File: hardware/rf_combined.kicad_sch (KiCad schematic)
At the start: 16 parts, among them J7 Conn_Coaxial, U1 PAT1220-C-3DB, U10 COS358SR, U2 PAT1220-C-3DB

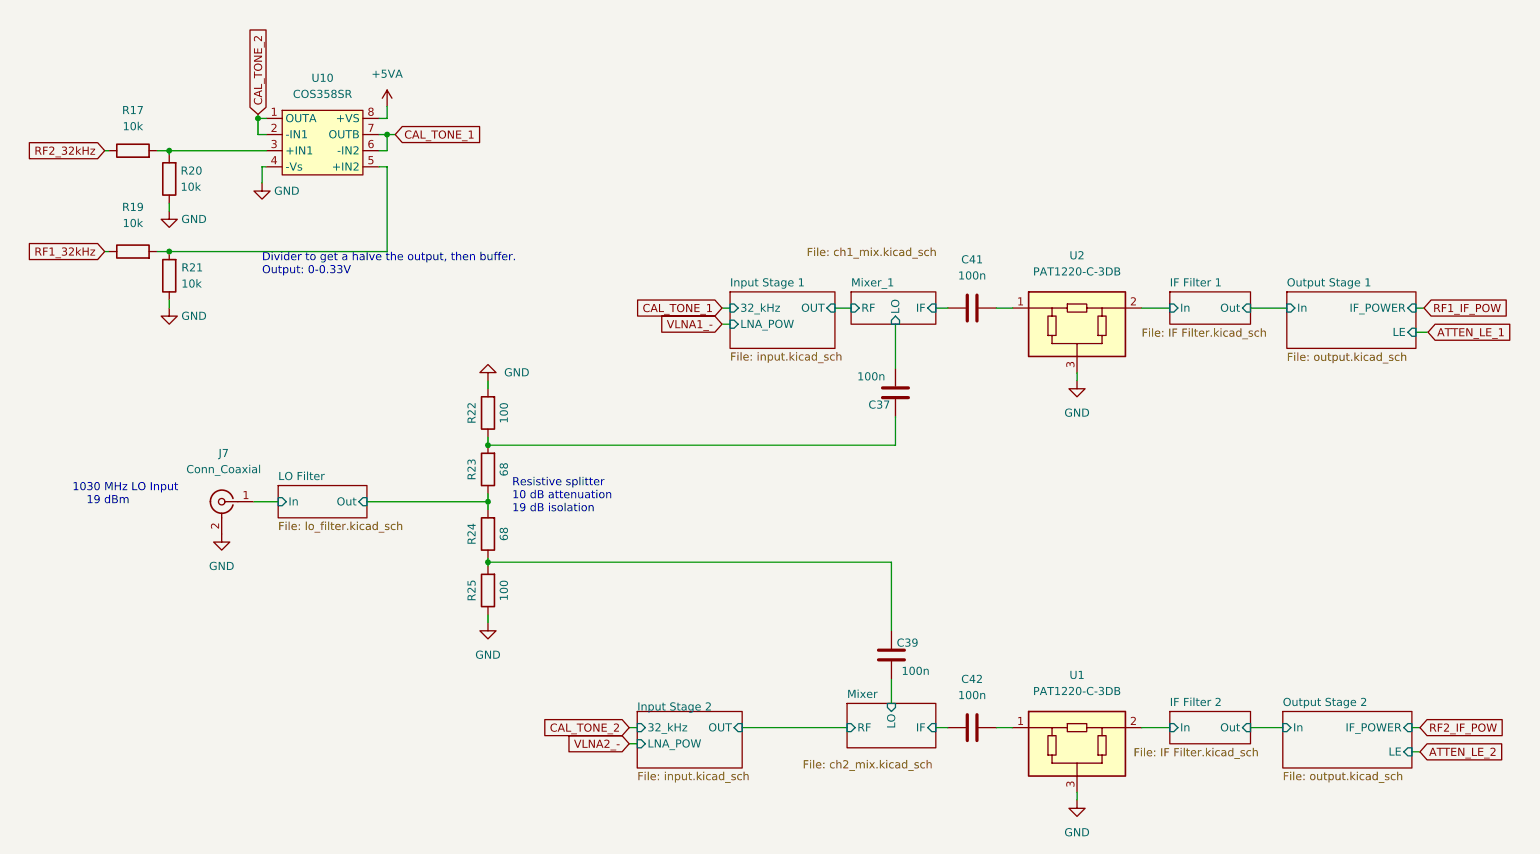
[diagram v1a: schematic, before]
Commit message: Remove cal circuit, swap attens, swap norflash
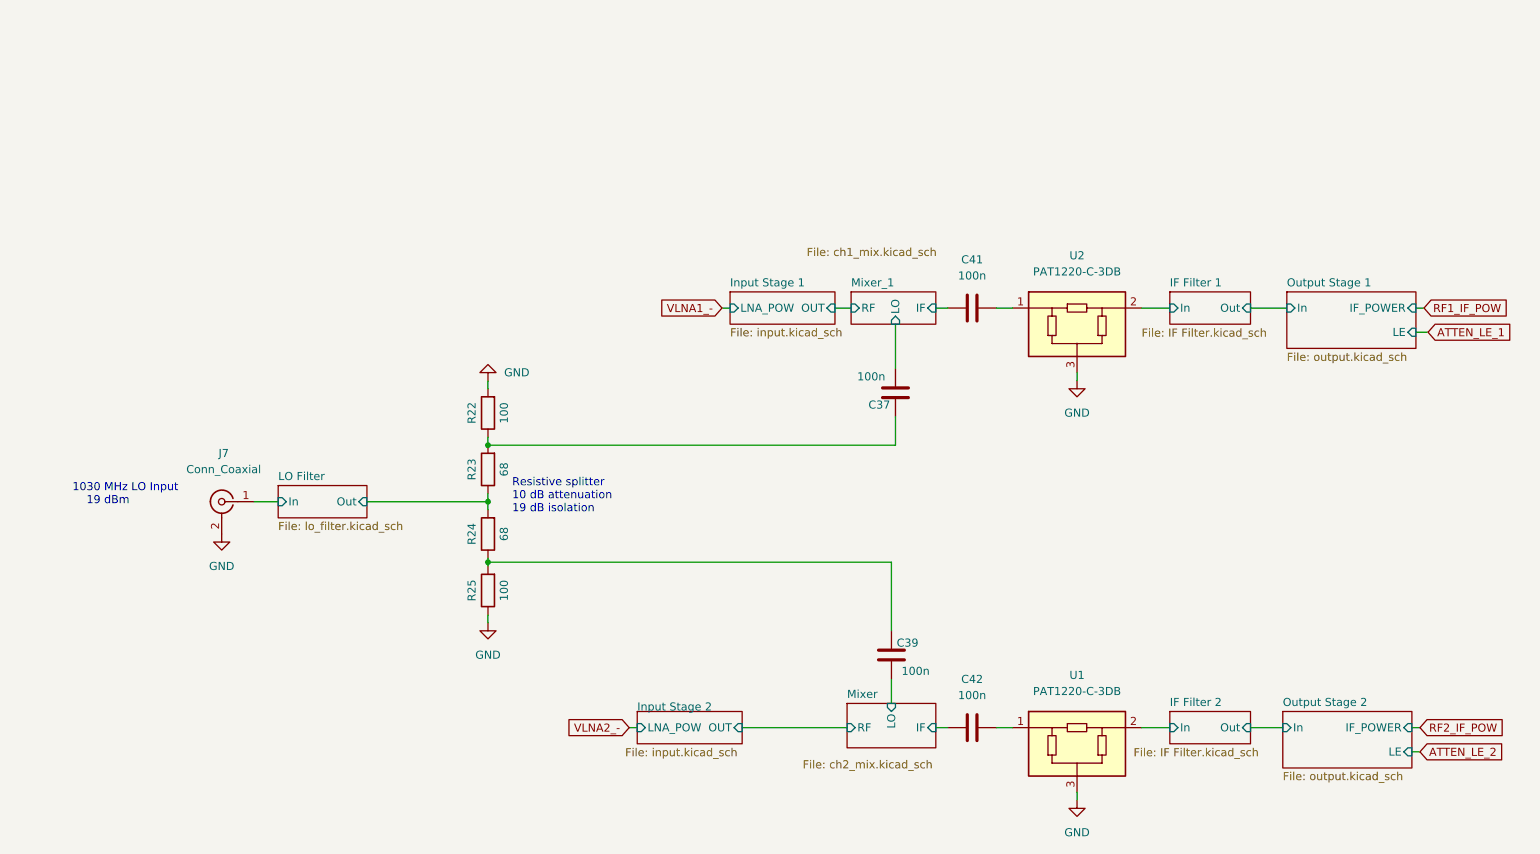
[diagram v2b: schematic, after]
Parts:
- removed R17, R19, R20, R21: 10k, Resistor_SMD:R_0402_1005Metric, symbol Device:R
- removed U10: COS358SR, Package_SO:SOP-8_3.9x4.9mm_P1.27mm, symbol Project Library:COS358SR
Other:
- sheet Input Stage 1 ports: added none; removed 32_kHz
- sheet Input Stage 2 ports: added none; removed 32_kHz
- note removed: "Divider to get a halve the output, then buffer. Output: 0-0.33V"

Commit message: Update FEM hardware design for production version
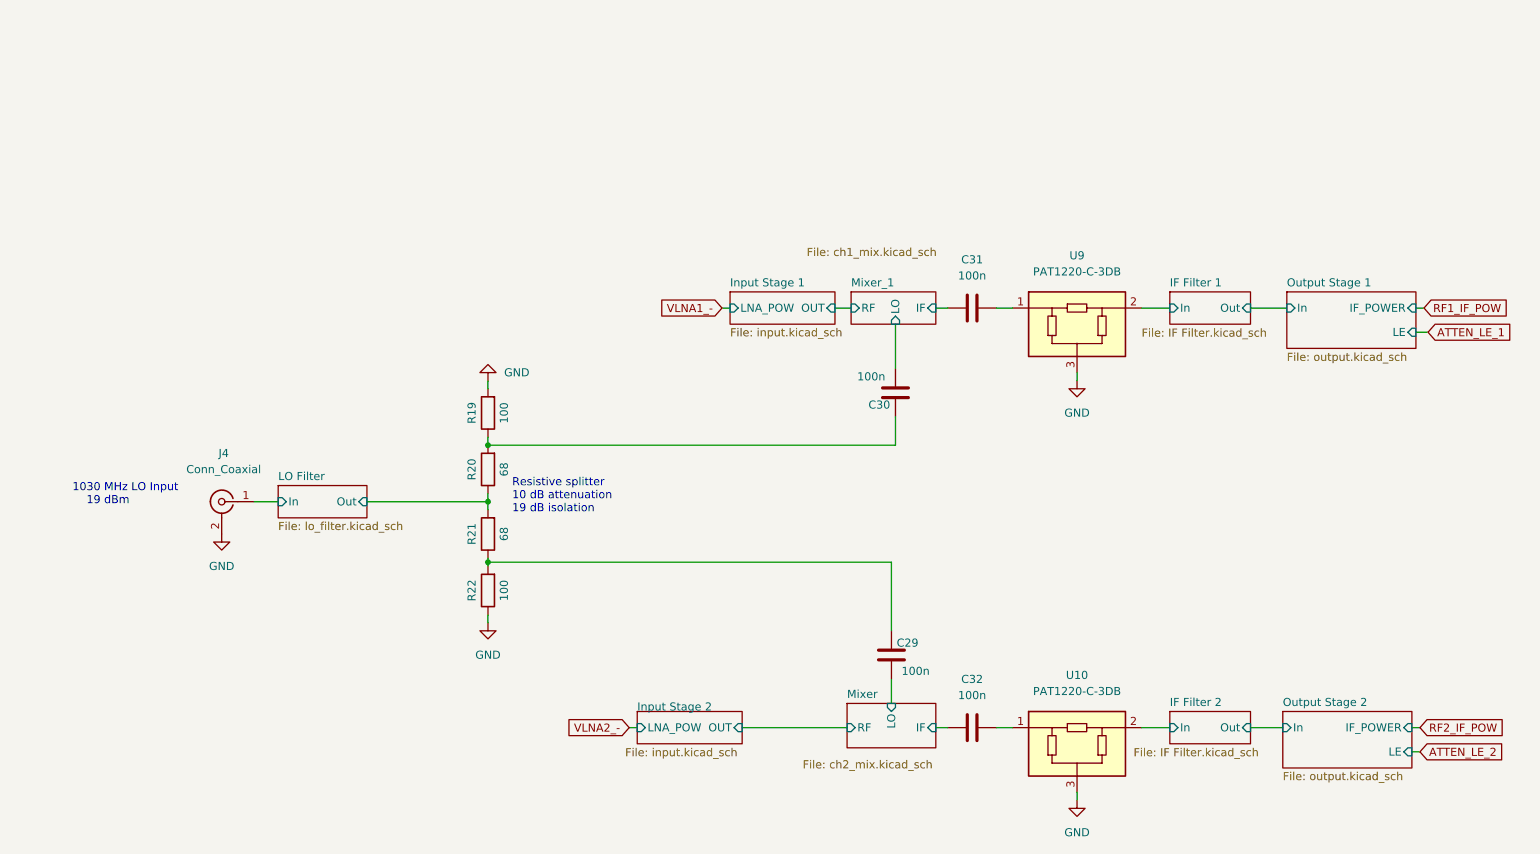
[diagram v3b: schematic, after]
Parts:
- renumbered C39 to C29, C37 to C30, C41 to C31, C42 to C32, J7 to J4, R22 to R19, R23 to R20, R24 to R21, R25 to R22, U1 to U10, U2 to U9
